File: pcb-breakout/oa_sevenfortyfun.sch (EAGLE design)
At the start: 46 parts, among them J1 1X01-TERM, J2 1X01-TERM, J3 1X01-TERM, J4 1X01-TERM, J5 1X01-TERM, J6 1X01-TERM, J7 1X01-TERM, J8 1X01-TERM, J9 2X04SHR, Q1 2N3904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

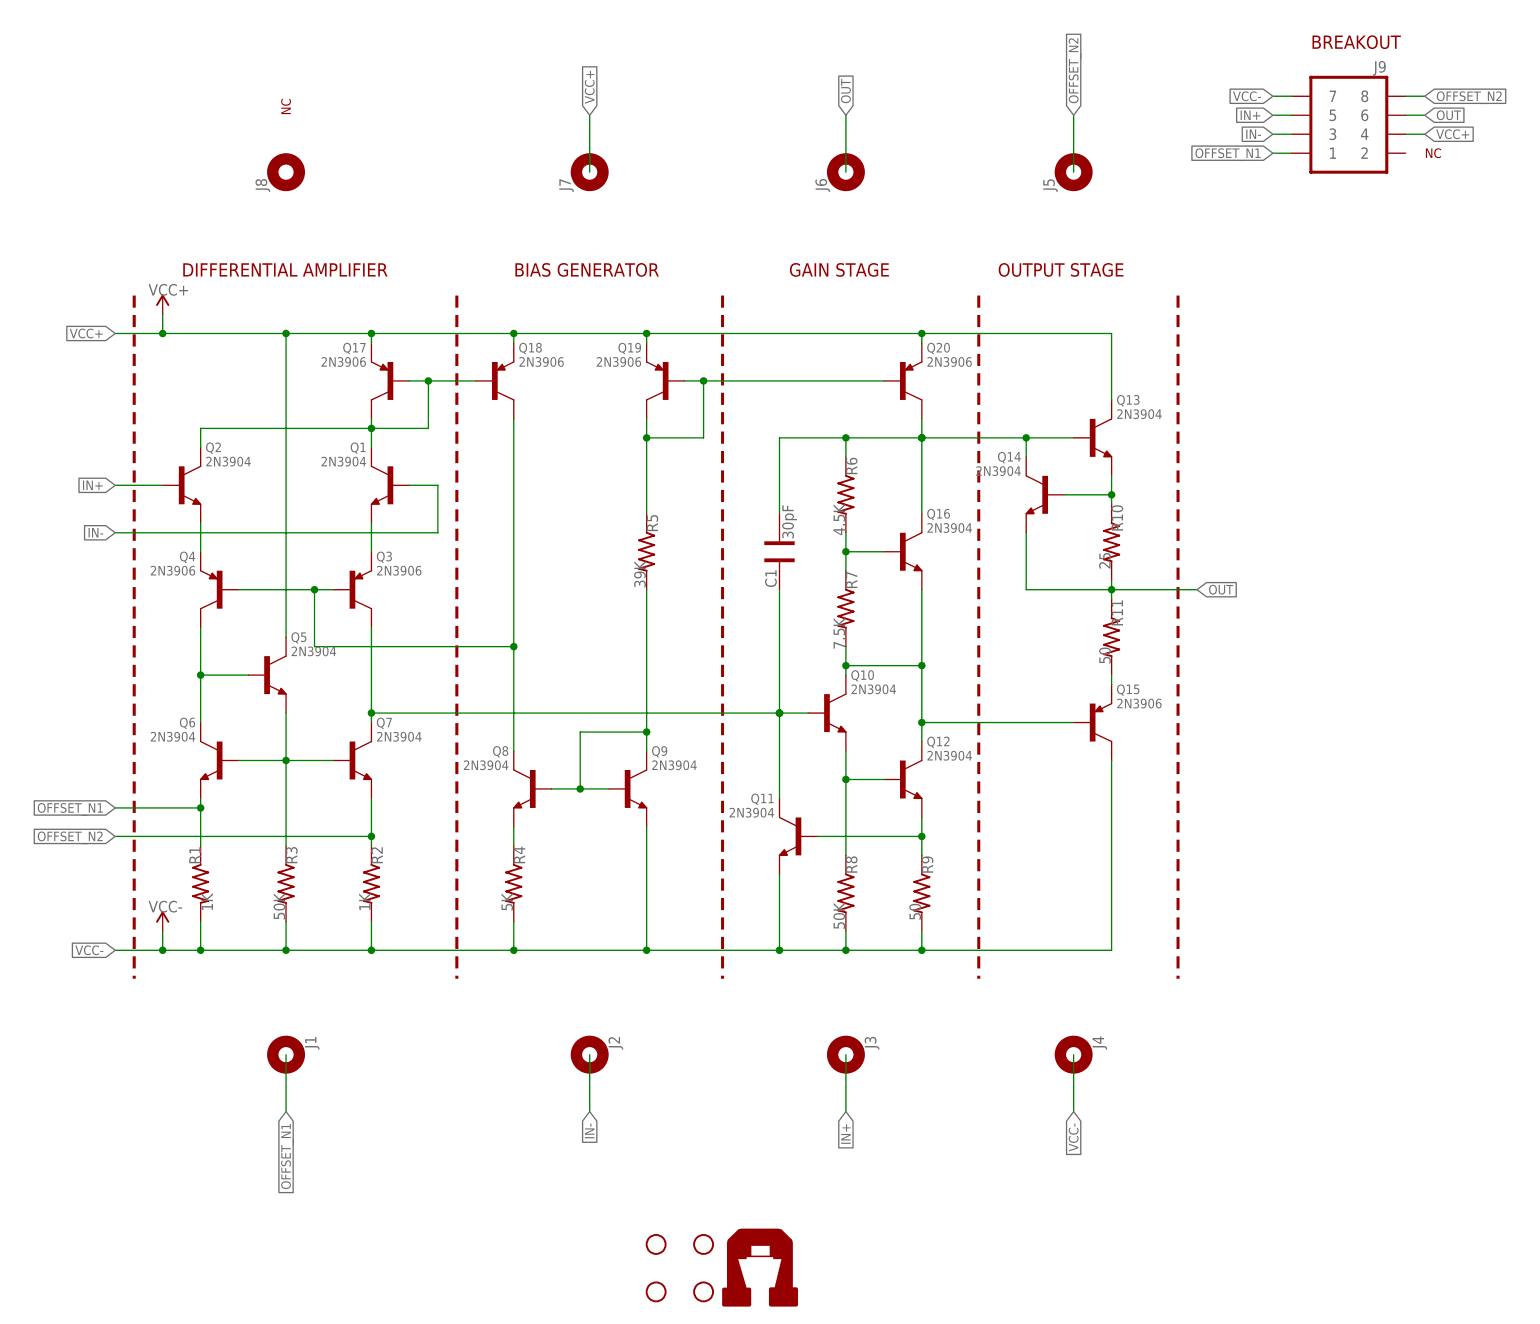
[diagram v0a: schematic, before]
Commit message: added breakout board
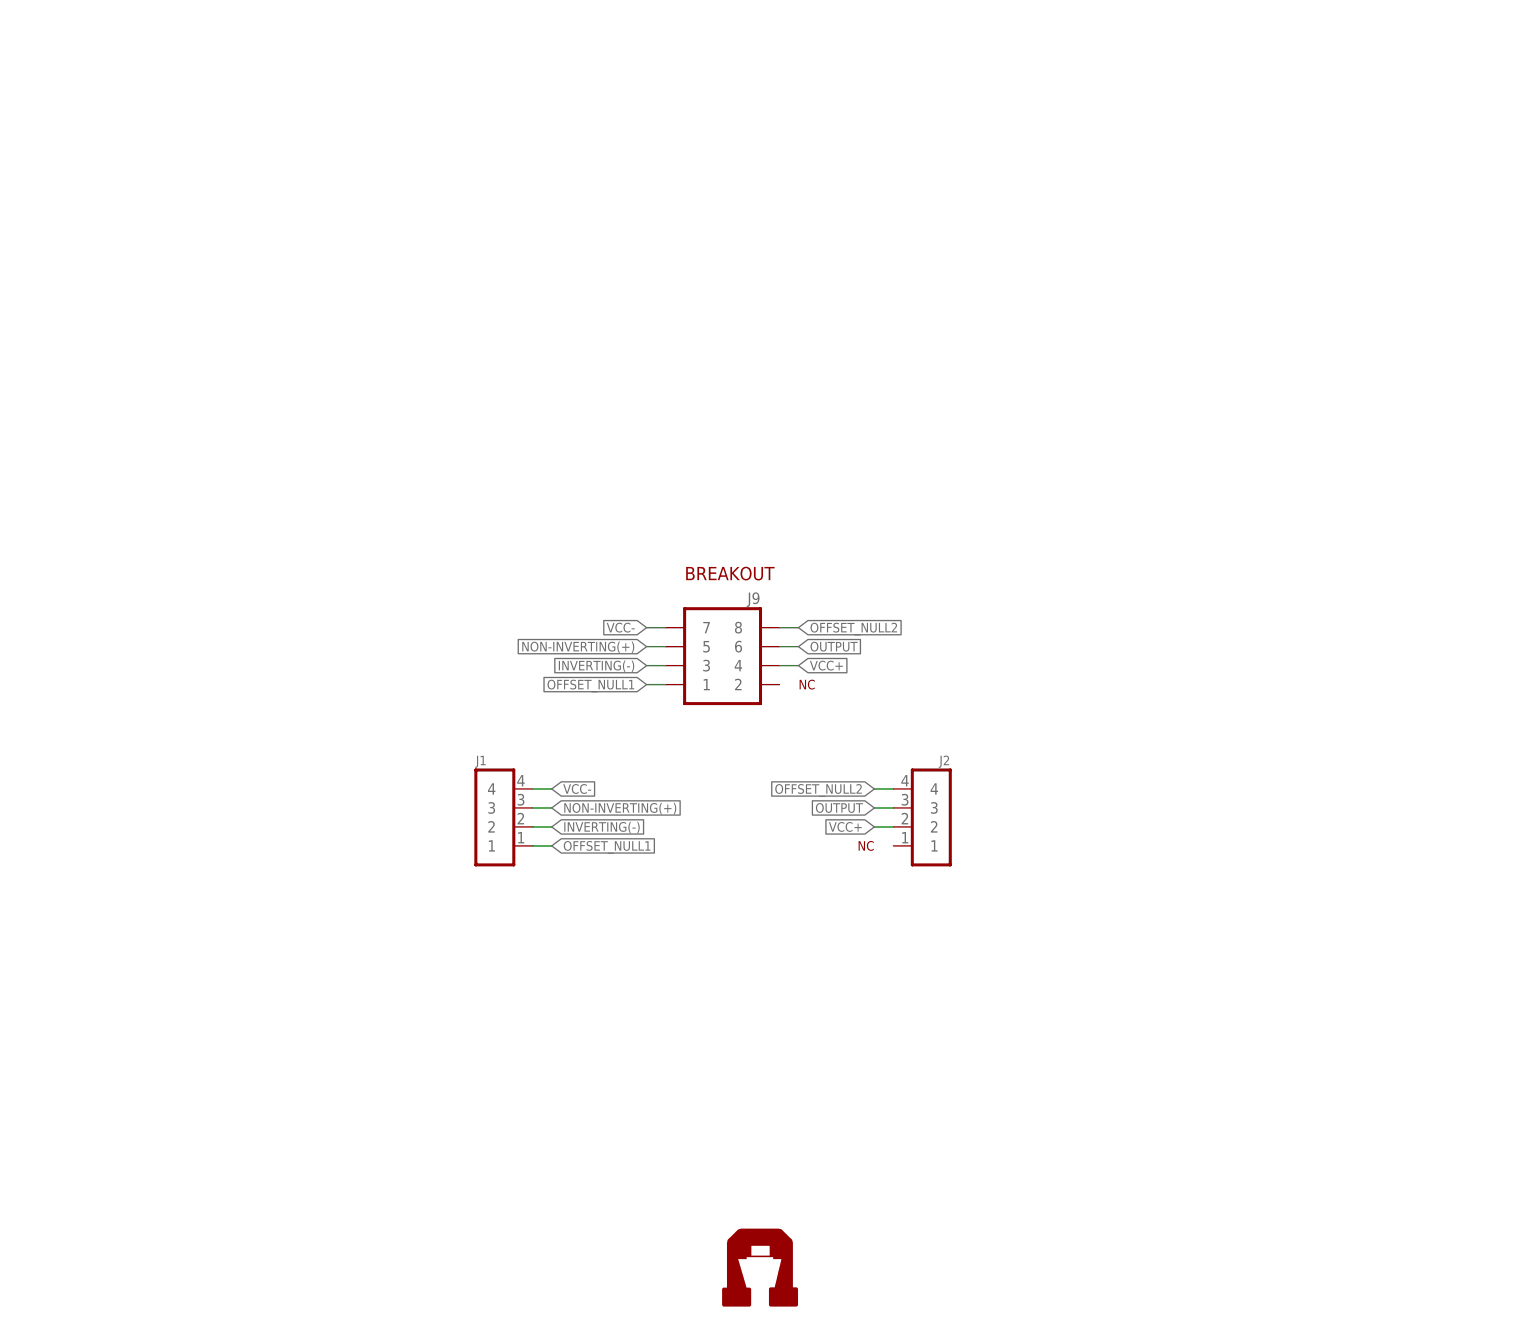
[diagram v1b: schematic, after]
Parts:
- removed C1: 30pF, Ai_Passives:CAP025X050
- removed J3, J4, J5, J6, J7, J8: 1X01-TERM, Ai_Connectors:1X01-TERM
- removed Q1, Q10, Q11, Q12, Q13, Q14, Q16, Q2, Q5, Q6, Q7, Q8, Q9: 2N3904, Ai_DiscreteSemis:TRANSISTOR-NPN
- removed Q15, Q17, Q18, Q19, Q20, Q3, Q4: 2N3906, Ai_DiscreteSemis:TRANSISTOR-PNP
- removed R1, R2: 1K, Ai_Passives:RESAXIAL-0.4
- removed R10: 25, Ai_Passives:RESAXIAL-0.4
- removed R11, R9: 50, Ai_Passives:RESAXIAL-0.4
- removed R3, R8: 50K, Ai_Passives:RESAXIAL-0.4
- removed R4: 5K, Ai_Passives:RESAXIAL-0.4
- removed R5: 39K, Ai_Passives:RESAXIAL-0.4
- removed R6: 4.5K, Ai_Passives:RESAXIAL-0.4
- removed R7: 7.5K, Ai_Passives:RESAXIAL-0.4
- removed STANDOFF1, STANDOFF2, STANDOFF3, STANDOFF4: STAND-OFF, Ai_Electromechanical:STAND-OFF
- J1: value 1X01-TERM -> 1X04NOSILK; device Ai_Connectors:1X01-TERM -> Ai_Connectors:1X04NOSILK
- J2: value 1X01-TERM -> 1X04NOFIRST; device Ai_Connectors:1X01-TERM -> Ai_Connectors:1X04NOFIRST
- U$3: value AI-LOGOL -> AI-LOGOXS; device Ai_Miscellany:AI-LOGOL -> Ai_Miscellany:AI-LOGOXS
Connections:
- removed net IN+: J3.1, J9.5, Q2.B
- removed net IN-: J2.1, J9.3, Q1.B
- removed net N$1: Q1.C, Q17.B, Q17.C, Q18.B, Q2.C
- removed net N$10: Q8.E, R4.1
- removed net N$14: Q10.E, Q12.B, R8.1
- removed net N$15: Q19.B, Q19.C, Q20.B, R5.1
- removed net N$16: Q8.B, Q9.B, Q9.C, R5.2
- removed net N$18: Q10.C, Q12.C, Q15.B, Q16.E, R7.2
- removed net N$19: Q16.B, R6.2, R7.1
- removed net N$2: Q2.E, Q4.E
- removed net N$21: Q11.B, Q12.E, R9.1
- removed net N$22: C1.1, Q13.B, Q14.C, Q16.C, Q20.C, R6.1
- removed net N$24: Q13.E, Q14.B, R10.1
- removed net N$3: Q1.E, Q3.E
- removed net N$4: Q4.C, Q5.B, Q6.C
- removed net N$5: C1.2, Q10.B, Q11.C, Q3.C, Q7.C
- removed net N$6: Q5.E, Q6.B, Q7.B, R3.1
- removed net N$7: Q15.E, R11.2
- removed net N$9: Q18.C, Q3.B, Q4.B, Q8.C
- removed net OFFSET_N1: J1.1, J9.1, Q6.E, R1.1
- removed net OFFSET_N2: J5.1, J9.8, Q7.E, R2.1
- removed net OUT: J6.1, J9.6, Q14.E, R10.2, R11.1
- new net INVERTING(-): J1.2, J9.3
- new net NON-INVERTING(+): J1.3, J9.5
- new net OFFSET_NULL1: J1.1, J9.1
- new net OFFSET_NULL2: J2.4, J9.8
- new net OUTPUT: J2.3, J9.6
- net VCC+: now also J2.2; no longer J7.1, Q13.C, Q17.E, Q18.E, Q19.E, Q20.E, Q5.C
- net VCC-: now also J1.4; no longer J4.1, Q11.E, Q15.C, Q9.E, R1.2, R2.2, R3.2, R4.2, R8.2, R9.2
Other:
- note removed: "BIAS GENERATOR"
- note removed: "DIFFERENTIAL AMPLIFIER"
- note removed: "GAIN STAGE"
- note removed: "OUTPUT STAGE"
- moved on the sheet: J9
